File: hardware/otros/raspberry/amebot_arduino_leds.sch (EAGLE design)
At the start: 16 parts

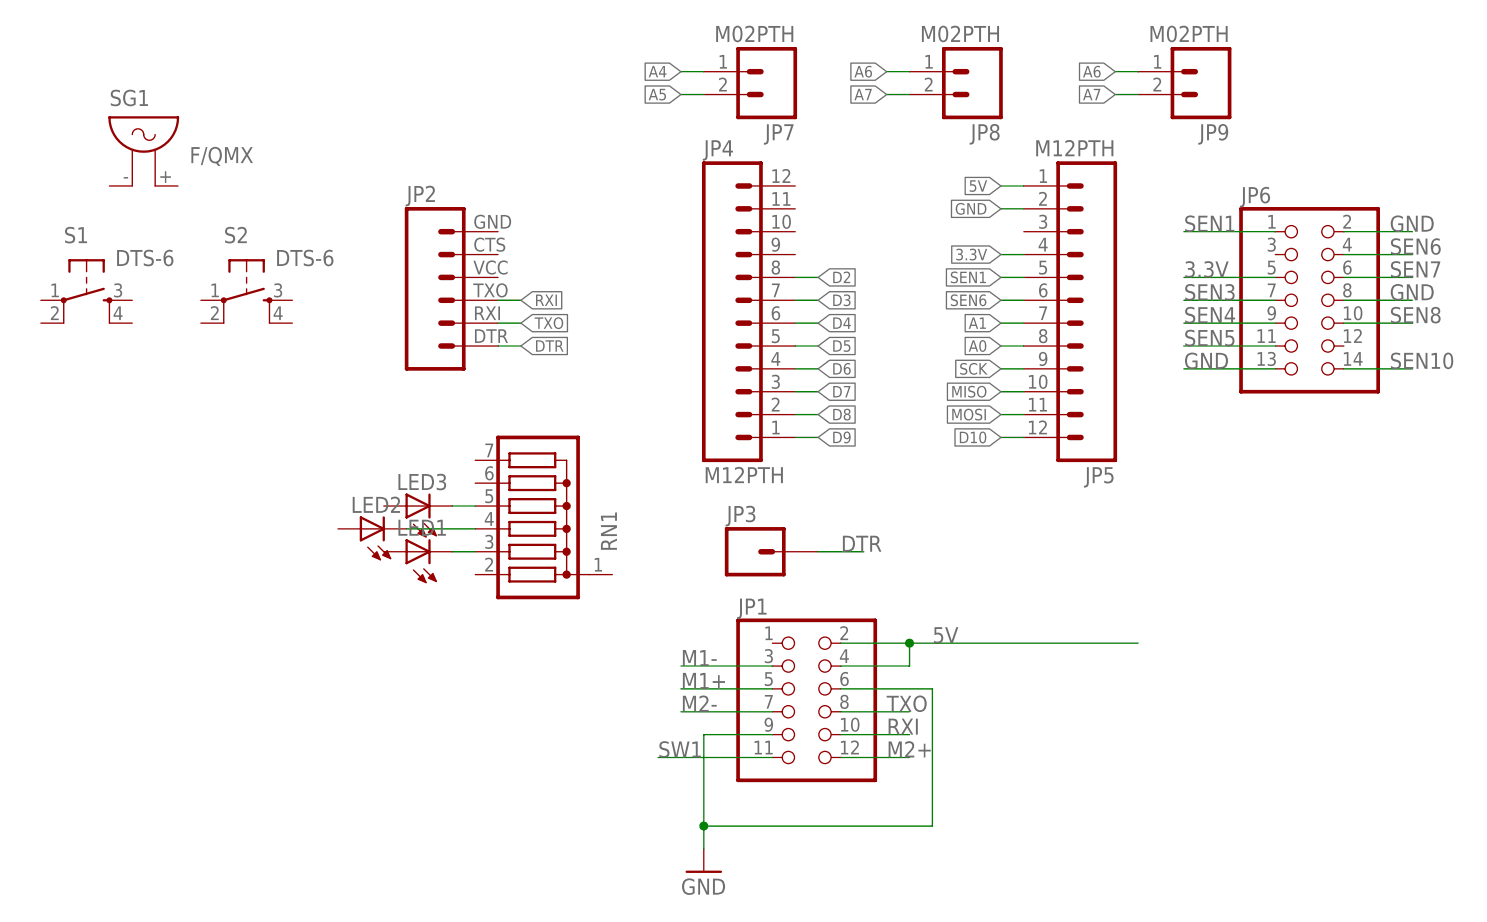
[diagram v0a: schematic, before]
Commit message: Añado cuarto led
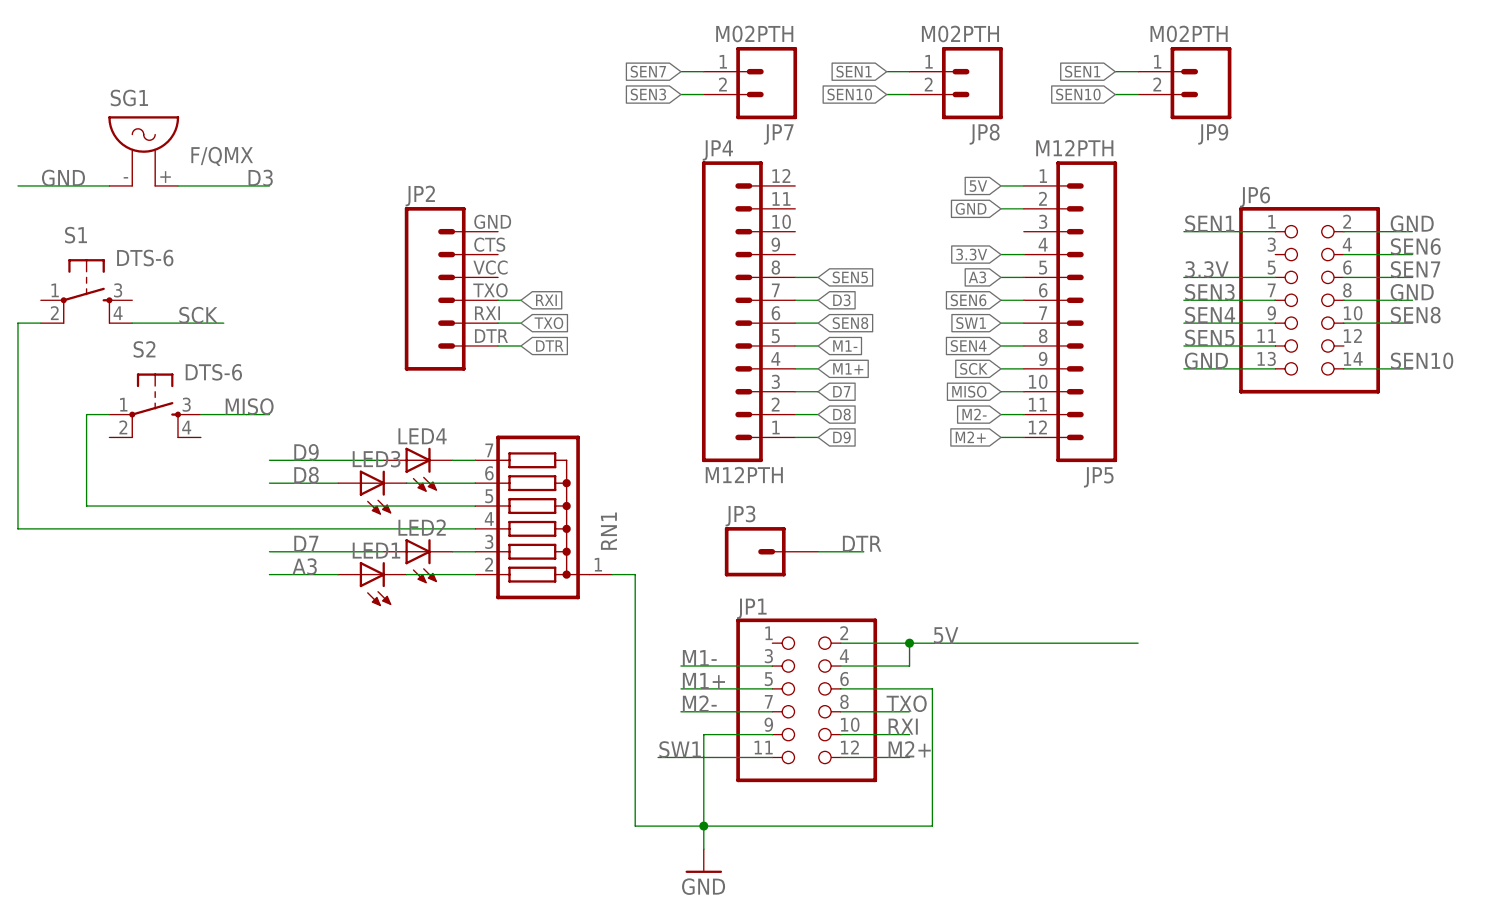
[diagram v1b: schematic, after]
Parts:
- added LED4: (no value), led:LED3MM
- LED1, LED2, LED3: device led:LED5MM -> led:LED3MM
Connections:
- removed net A0: JP5.8
- removed net A1: JP5.7
- removed net A4: JP7.1
- removed net A5: JP7.2
- removed net A6: JP8.1, JP9.1
- removed net A7: JP8.2, JP9.2
- removed net D10: JP5.12
- removed net D2: JP4.8
- removed net D4: JP4.6
- removed net D5: JP4.5
- removed net D6: JP4.4
- removed net MOSI: JP5.11
- new net A3: JP5.5, LED1.A
- new net N$4: LED3.C, RN1.6
- new net N$7: RN1.4, S1.2
- new net N$9: RN1.5, S2.1
- net D3: now also SG1.2
- net D7: now also LED2.A
- net D8: now also LED3.A
- net D9: now also LED4.A
- net GND: now also RN1.1, SG1.1
- net M1+: now also JP4.4
- net M1-: now also JP4.5
- net M2+: now also JP5.12
- net M2-: now also JP5.11
- net MISO: now also S2.3
- net N$1: now also LED2.C; no longer LED1.C
- net N$2: now also LED1.C, RN1.2; no longer LED2.C, RN1.4
- net N$3: now also LED4.C, RN1.7; no longer LED3.C, RN1.5
- net SCK: now also S1.4
- net SEN1: now also JP8.1, JP9.1; no longer JP5.5
- net SEN10: now also JP8.2, JP9.2
- net SEN3: now also JP7.2
- net SEN4: now also JP5.8
- net SEN5: now also JP4.8
- net SEN7: now also JP7.1
- net SEN8: now also JP4.6
- net SW1: now also JP5.7
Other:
- moved on the sheet: LED1, LED2, LED3, S2
